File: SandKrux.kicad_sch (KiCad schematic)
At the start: 119 parts, among them CN2 1.25mm-2P socket, IC1 TROPIC01_chip, Q1 S8050, Q2 SI2301CDS-T1-GE3, SW1 TL3330AF130QG, SW2 TL3330AF130QG, SW3 TL3330AF130QG, SW4 TL3330AF130QG, SW5 TL3330AF130QG, U10 AXP173_C3345106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

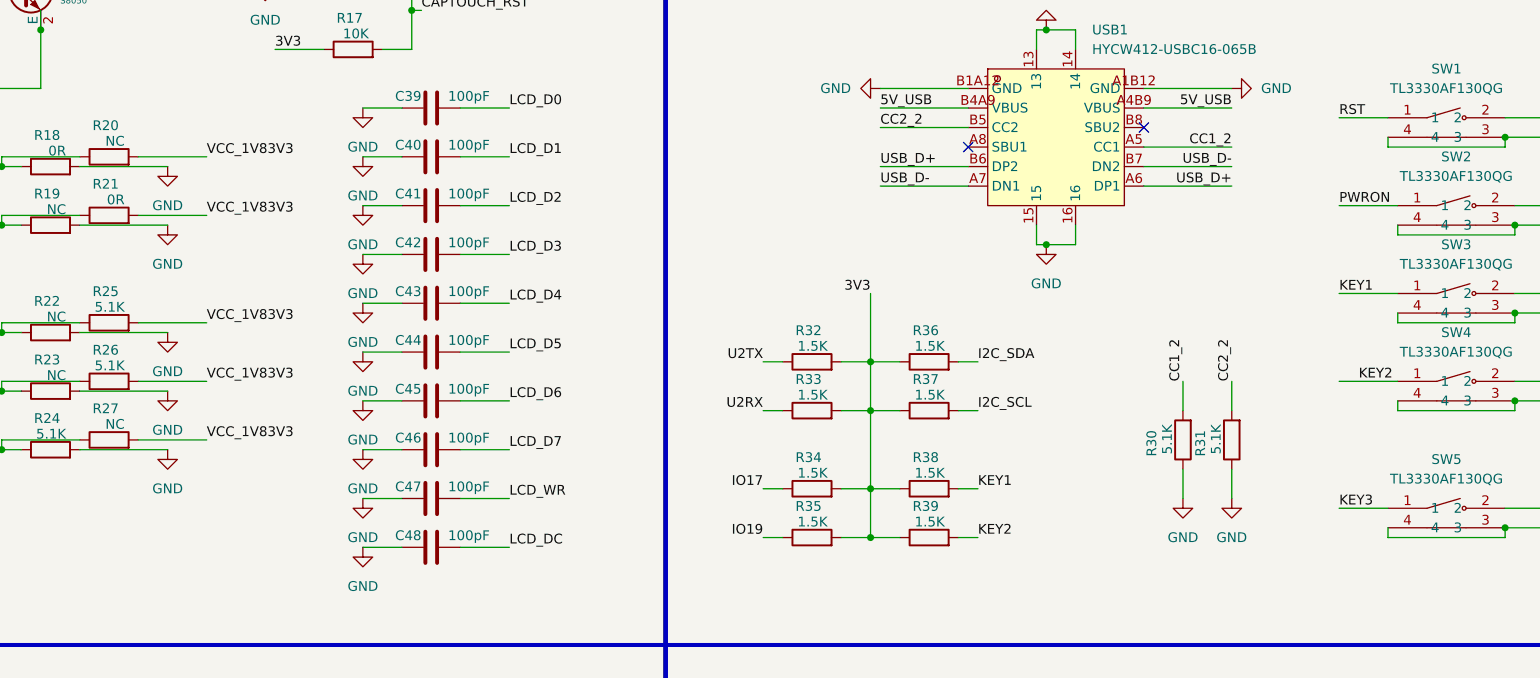
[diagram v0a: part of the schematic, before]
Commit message: lcd and bottons conection on board
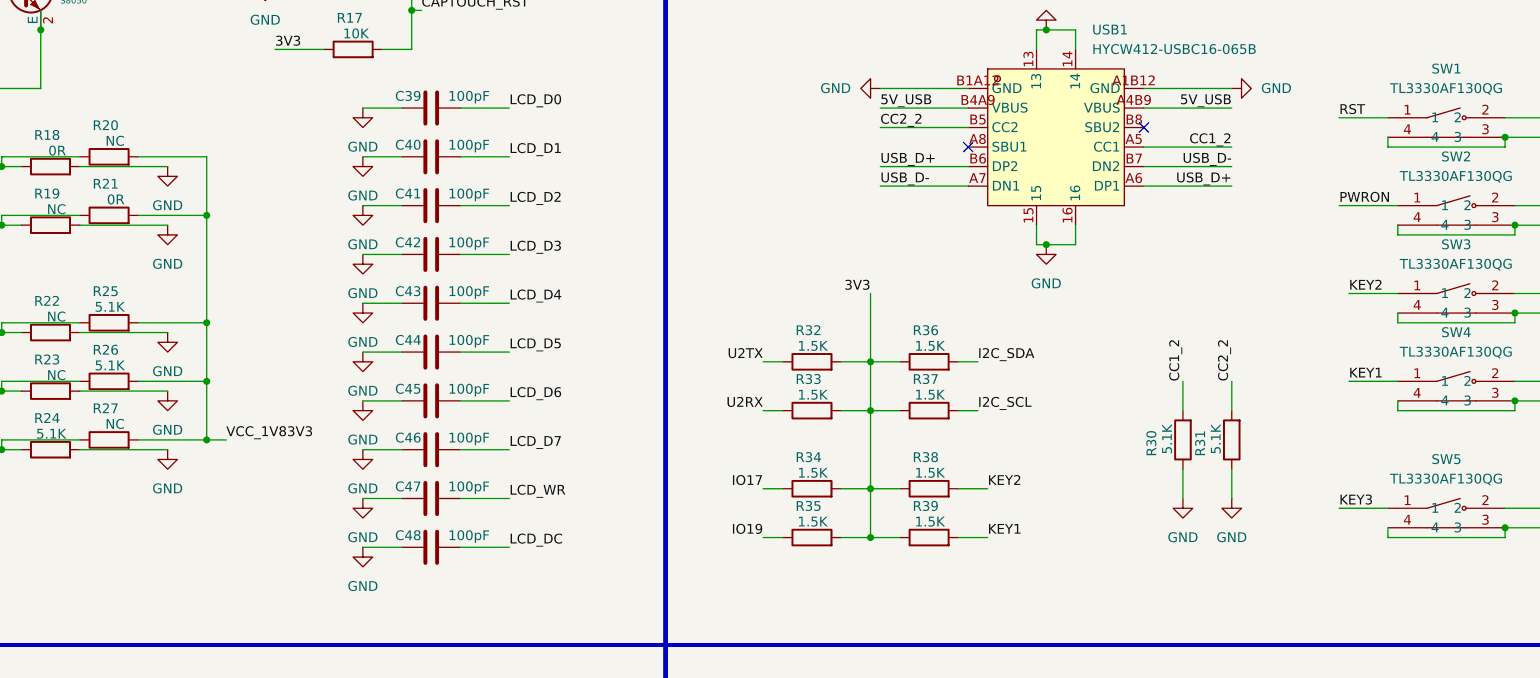
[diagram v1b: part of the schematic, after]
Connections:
- net KEY1: now also R39.2, SW4.1; no longer R38.2, SW3.1
- net KEY2: now also R38.2, SW3.1; no longer R39.2, SW4.1
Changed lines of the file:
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@@
 	)
 	(junction
+		(at 374.65 128.27)
+		(diameter 0)
+		(color 0 0 0 0)
+	)
+	(junction
 		(at 513.08 199.39)
 		(diameter 0)
@@
 	)
 	(junction
+		(at 374.65 106.68)
+		(diameter 0)
+		(color 0 0 0 0)
+	)
+	(junction
 		(at 543.56 147.32)
 		(diameter 0)
@@
 	)
 	(junction
+		(at 374.65 135.89)
+		(diameter 0)
+		(color 0 0 0 0)
+	)
+	(junction
 		(at 283.21 196.85)
 		(diameter 0)
@@
 		(color 0 0 0 0)
 	)
+	(junction
+		(at 374.65 120.65)
+		(diameter 0)
+		(color 0 0 0 0)
+	)
 	(no_connect
 		(at 162.56 39.37)
@@
 	(wire
 		(pts
-			(xy 472.44 142.24) (xy 474.98 142.24)
-		)
-		(stroke
-			(width 0)
-			(type default)
-		)
-	)
-	(wire
-		(pts
 			(xy 513.08 199.39) (xy 515.62 199.39)
 		)
@@
 	(wire
 		(pts
+			(xy 523.24 128.27) (xy 529.59 128.27)
+		)
+		(stroke
+			(width 0)
+			(type default)
+		)
+	)
+	(wire
+		(pts
 			(xy 341.63 229.87) (xy 359.41 229.87)
 		)
@@
 	(wire
 		(pts
+			(xy 377.19 135.89) (xy 374.65 135.89)
+		)
+		(stroke
+			(width 0)
+			(type default)
+		)
+	)
+	(wire
+		(pts
 			(xy 543.56 96.52) (xy 551.18 96.52)
 		)
@@
 	(wire
 		(pts
-			(xy 521.97 116.84) (xy 529.59 116.84)
+			(xy 461.01 142.24) (xy 461.01 148.59)
 		)
 		(stroke
@@
 	(wire
 		(pts
-			(xy 461.01 142.24) (xy 461.01 148.59)
+			(xy 388.62 44.45) (xy 392.43 44.45)
 		)
 		(stroke
@@
 	(wire
 		(pts
-			(xy 388.62 44.45) (xy 392.43 44.45)
+			(xy 397.51 76.2) (xy 401.32 76.2)
 		)
 		(stroke
@@
 	(wire
 		(pts
-			(xy 397.51 76.2) (xy 401.32 76.2)
+			(xy 394.97 92.71) (xy 400.05 92.71)
 		)
 		(stroke
@@
 	(wire
 		(pts
-			(xy 394.97 92.71) (xy 400.05 92.71)
+			(xy 462.28 90.17) (xy 473.71 90.17)
 		)
 		(stroke
@@
 	(wire
 		(pts
-			(xy 462.28 90.17) (xy 473.71 90.17)
+			(xy 472.44 148.59) (xy 476.25 148.59)
 		)
 		(stroke
@@
 	(wire
 		(pts
+			(xy 472.44 142.24) (xy 476.25 142.24)
+		)
+		(stroke
+			(width 0)
+			(type default)
+		)
+	)
+	(wire
+		(pts
 			(xy 303.53 77.47) (xy 312.42 77.47)
 		)
@@
 	(wire
 		(pts
+			(xy 523.24 116.84) (xy 529.59 116.84)
+		)
+		(stroke
+			(width 0)
+			(type default)
+		)
+	)
+	(wire
+		(pts
 			(xy 349.25 201.93) (xy 359.41 201.93)
 		)
@@
 	(wire
 		(pts
-			(xy 303.53 82.55) (xy 312.42 82.55)
-		)
-		(stroke
-			(width 0)
-			(type default)
-		)
-	)
-	(wire
-		(pts
 			(xy 356.87 208.28) (xy 359.41 208.28)
 		)
@@
 	(wire
 		(pts
-			(xy 118.11 109.22) (xy 113.03 109.22)
+			(xy 374.65 120.65) (xy 374.65 128.27)
 		)
 		(stroke
@@
 	(wire
 		(pts
-			(xy 187.96 69.85) (xy 194.31 69.85)
+			(xy 118.11 109.22) (xy 113.03 109.22)
 		)
 		(stroke
@@
 	(wire
 		(pts
-			(xy 425.45 40.64) (xy 427.99 40.64)
+			(xy 187.96 69.85) (xy 194.31 69.85)
 		)
 		(stroke
@@
 	(wire
 		(pts
-			(xy 365.76 135.89) (xy 374.65 135.89)
+			(xy 425.45 40.64) (xy 427.99 40.64)
 		)
 		(stroke
@@
 	(wire
 		(pts
+			(xy 374.65 99.06) (xy 374.65 106.68)
+		)
+		(stroke
+			(width 0)
+			(type default)
+		)
+	)
+	(wire
+		(pts
 			(xy 347.98 264.16) (xy 341.63 264.16)
 		)
@@
 	(wire
 		(pts
+			(xy 374.65 128.27) (xy 374.65 135.89)
+		)
+		(stroke
+			(width 0)
+			(type default)
+		)
+	)
+	(wire
+		(pts
 			(xy 306.07 246.38) (xy 283.21 246.38)
 		)
@@
 	(wire
 		(pts
-			(xy 521.97 128.27) (xy 529.59 128.27)
-		)
-		(stroke
-			(width 0)
-			(type default)
-		)
-	)
-	(wire
-		(pts
 			(xy 557.53 144.78) (xy 557.53 151.13)
 		)
@@
 	(wire
 		(pts
-			(xy 472.44 148.59) (xy 474.98 148.59)
-		)
-		(stroke
-			(width 0)
-			(type default)
-		)
-	)
-	(wire
-		(pts
 			(xy 359.41 198.12) (xy 360.68 198.12)
 		)
@@
 	(wire
 		(pts
+			(xy 374.65 106.68) (xy 374.65 120.65)
+		)
+		(stroke
+			(width 0)
+			(type default)
+		)
+	)
+	(wire
+		(pts
 			(xy 107.95 67.31) (xy 137.16 67.31)
 		)
@@
 	(wire
 		(pts
+			(xy 303.53 82.55) (xy 312.42 82.55)
+		)
+		(stroke
+			(width 0)
+			(type default)
+		)
+	)
+	(wire
+		(pts
 			(xy 510.54 250.19) (xy 508 250.19)
 		)
@@
 	(wire
 		(pts
+			(xy 374.65 135.89) (xy 365.76 135.89)
+		)
+		(stroke
+			(width 0)
+			(type default)
+		)
+	)
+	(wire
+		(pts
 			(xy 95.25 30.48) (xy 106.68 30.48)
 		)
@@
 		)
 	)
-	(label "VCC_1V83V3"
-		(at 374.65 128.27 0)
-		(effects
-			(font
-				(size 1.27 1.27)
-			)
-			(justify left bottom)
-		)
-	)
 	(label "USB_D+"
 		(at 462.28 100.33 0)
@@
 	)
 	(label "KEY2"
-		(at 474.98 148.59 0)
+		(at 476.25 142.24 0)
 		(effects
 			(font
@@
 	)
 	(label "KEY1"
-		(at 521.97 116.84 0)
+		(at 523.24 128.27 0)
 		(effects
 			(font
@@
 	)
 	(label "KEY2"
-		(at 524.51 128.27 0)
+		(at 523.24 116.84 0)
 		(effects
 			(font
@@
 	)
 	(label "VCC_1V83V3"
-		(at 374.65 135.89 0)
+		(at 377.19 135.89 0)
 		(effects
 			(font
@@
 		)
 	)
-	(label "VCC_1V83V3"
-		(at 374.65 120.65 0)
-		(effects
-			(font
-				(size 1.27 1.27)
-			)
-			(justify left bottom)
-		)
-	)
 	(label "24M_OUT"
 		(at 130.81 62.23 180)
@@
 		)
 	)
-	(label "VCC_1V83V3"
-		(at 374.65 106.68 0)
-		(effects
-			(font
-				(size 1.27 1.27)
-			)
-			(justify left bottom)
-		)
-	)
-	(label "VCC_1V83V3"
-		(at 374.65 99.06 0)
-		(effects
-			(font
-				(size 1.27 1.27)
-			)
-			(justify left bottom)
-		)
-	)
 	(label "GD_PA1"
 		(at 130.81 72.39 180)
@@
 	)
 	(label "KEY1"
-		(at 474.98 142.24 0)
+		(at 476.25 148.59 0)
 		(effects
 			(font

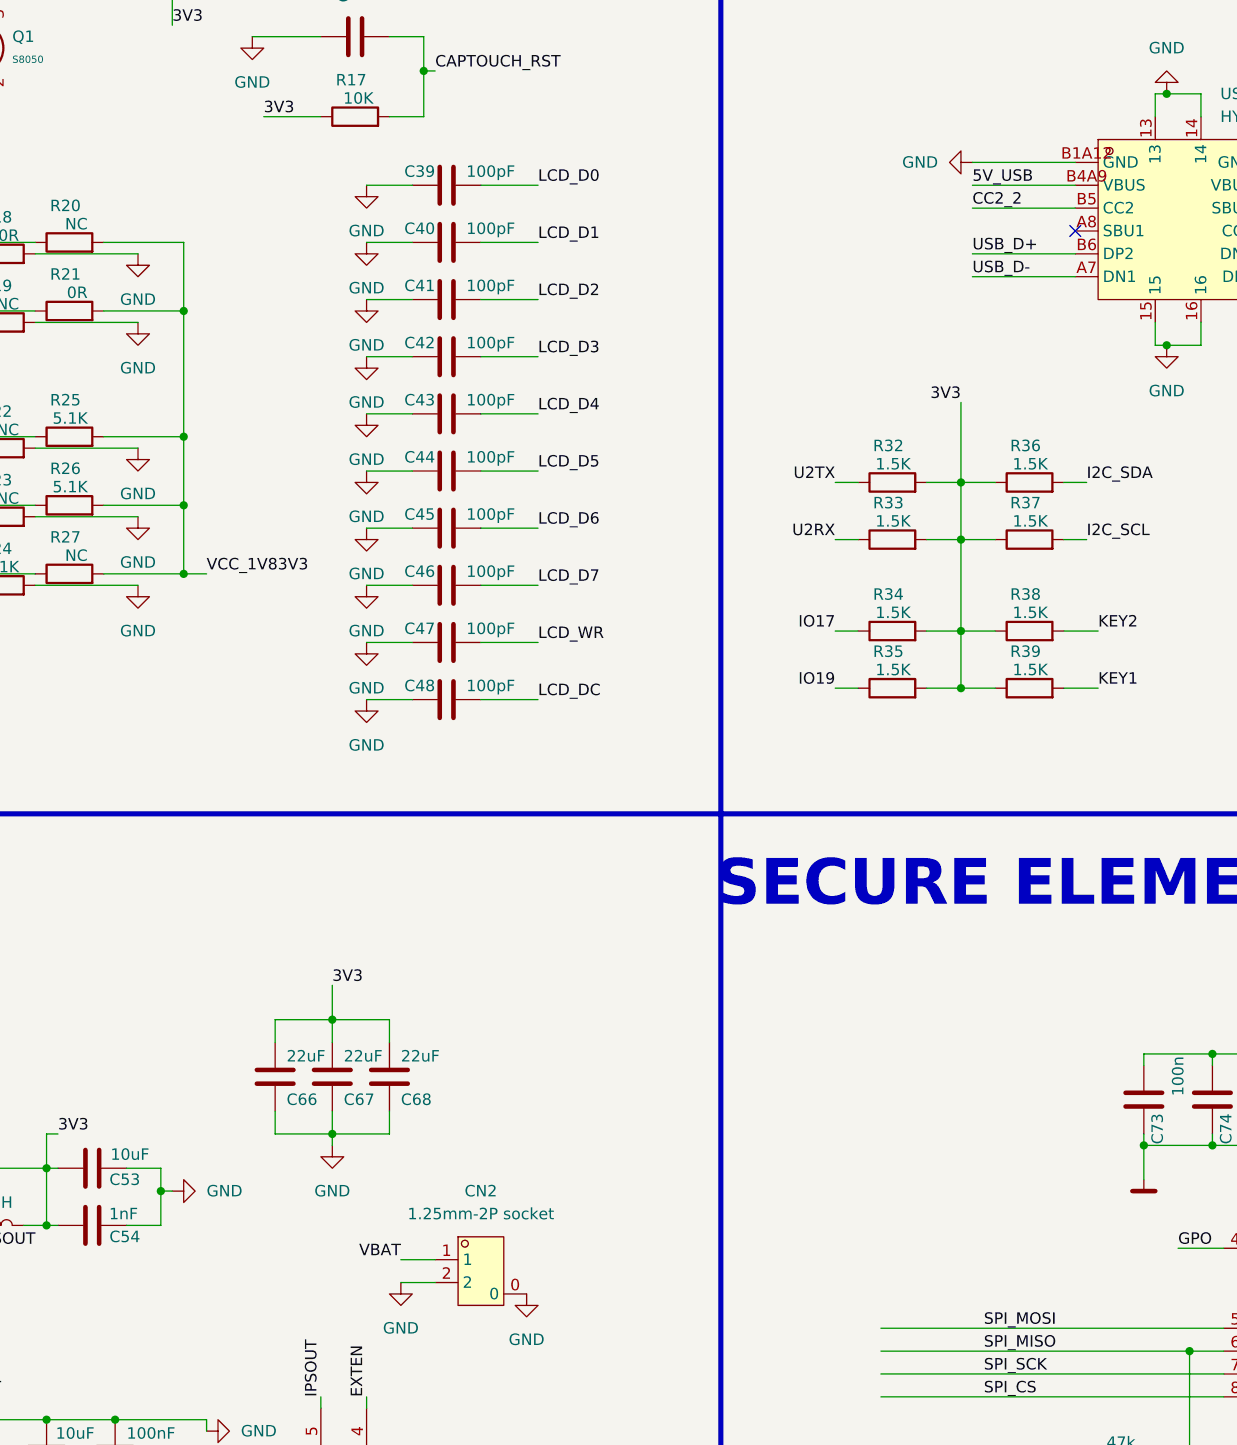
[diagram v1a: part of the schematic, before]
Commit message: test points and traces distribution
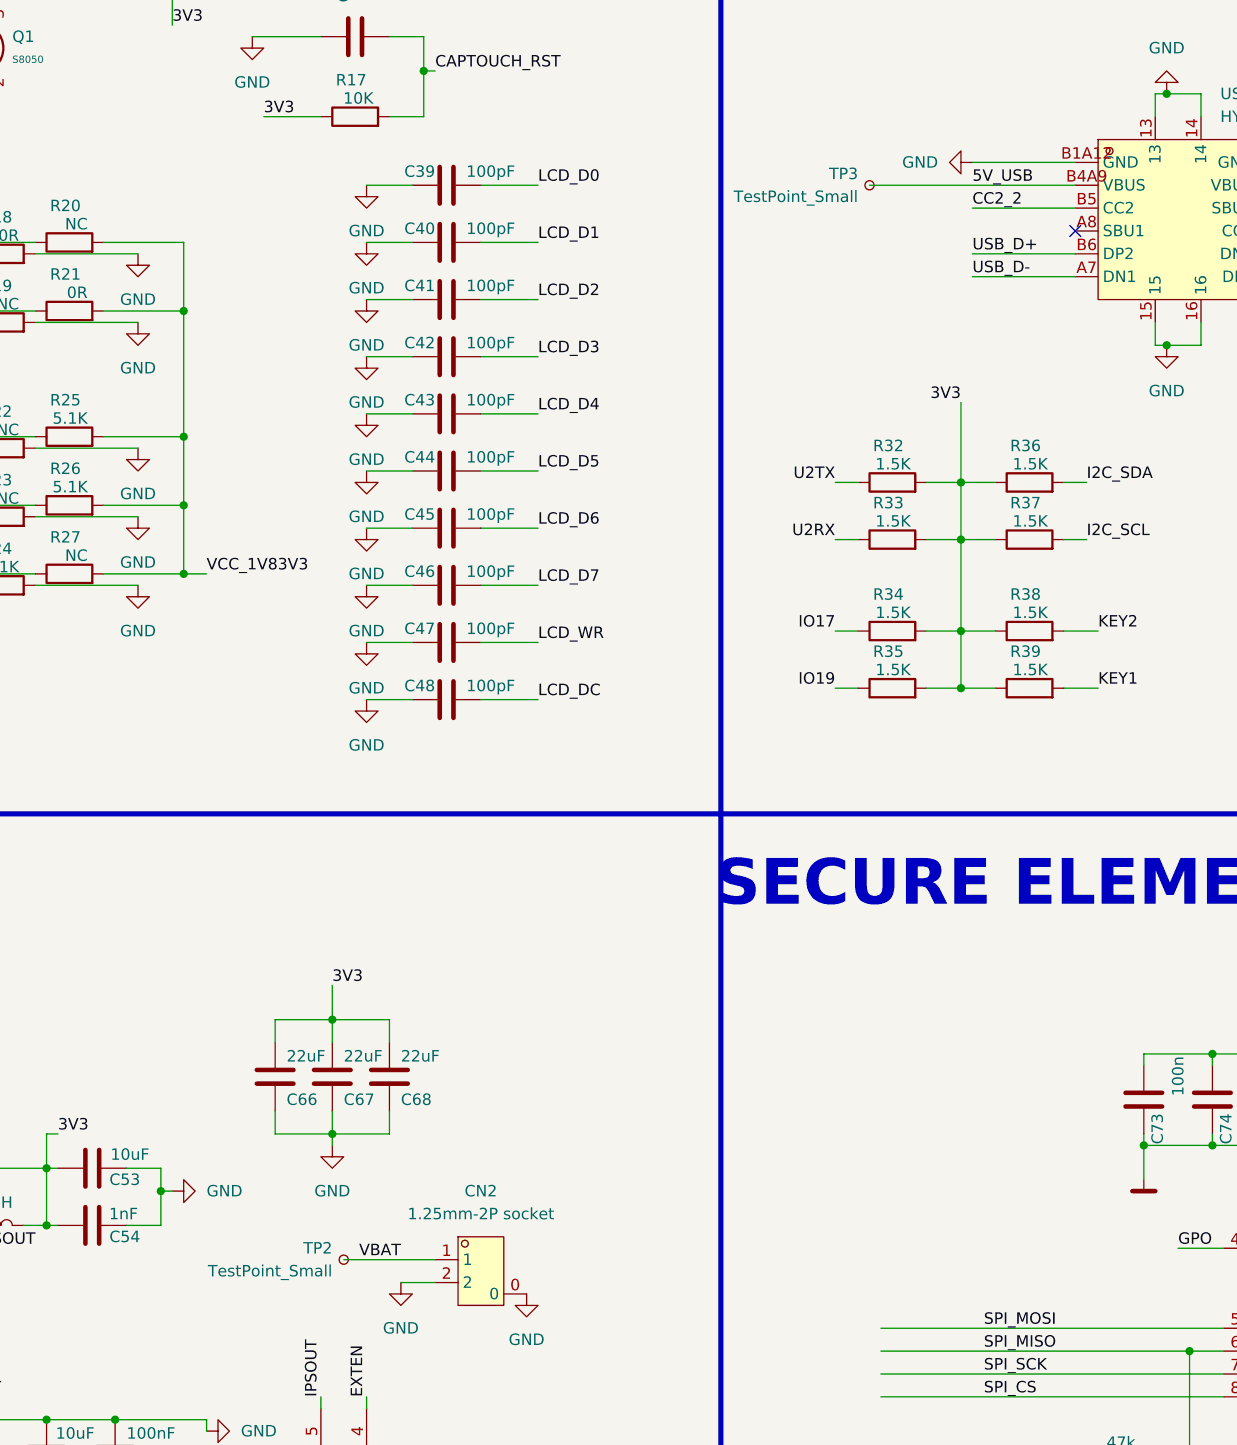
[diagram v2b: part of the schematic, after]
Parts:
- added TP2, TP3: TestPoint_Small, TestPoint:TestPoint_Pad_D1.0mm, symbol Connector:TestPoint_Small
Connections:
- net 5V_USB: now also TP3.1
- net VBAT: now also TP2.1
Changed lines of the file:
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@@
 	(wire
 		(pts
-			(xy 398.78 212.09) (xy 402.59 212.09)
-		)
-		(stroke
-			(width 0)
-			(type default)
-		)
-	)
-	(wire
-		(pts
 			(xy 283.21 205.74) (xy 283.21 204.47)
 		)
@@
 	(wire
 		(pts
+			(xy 392.43 212.09) (xy 402.59 212.09)
+		)
+		(stroke
+			(width 0)
+			(type default)
+		)
+	)
+	(wire
+		(pts
 			(xy 518.16 250.19) (xy 515.62 250.19)
 		)
@@
 	(wire
 		(pts
+			(xy 450.85 92.71) (xy 473.71 92.71)
+		)
+		(stroke
+			(width 0)
+			(type default)
+		)
+	)
+	(wire
+		(pts
 			(xy 170.18 90.17) (xy 170.18 99.06)
 		)
@@
 	(wire
 		(pts
-			(xy 462.28 92.71) (xy 473.71 92.71)
-		)
-		(stroke
-			(width 0)
-			(type default)
-		)
-	)
-	(wire
-		(pts
 			(xy 359.41 201.93) (xy 359.41 208.28)
 		)
@@
 	)
 	(symbol
+		(lib_id "Connector:TestPoint_Small")
+		(at 450.85 92.71 0)
+		(mirror y)
+		(unit 1)
+		(exclude_from_sim no)
+		(in_bom yes)
+		(on_board yes)
+		(dnp no)
+		(property "Reference" "TP3"
+			(at 449.58 91.4399 0)
+			(effects
+				(font
+					(size 1.27 1.27)
+				)
+				(justify left)
+			)
+		)
+		(property "Value" "TestPoint_Small"
+			(at 449.58 93.9799 0)
+			(effects
+				(font
+					(size 1.27 1.27)
+				)
+				(justify left)
+			)
+		)
+		(property "Footprint" "TestPoint:TestPoint_Pad_D1.0mm"
+			(at 445.77 92.71 0)
+			(effects
+				(font
+					(size 1.27 1.27)
+				)
+				(hide yes)
+			)
+		)
+		(property "Datasheet" "~"
+			(at 445.77 92.71 0)
+			(effects
+				(font
+					(size 1.27 1.27)
+				)
+				(hide yes)
+			)
+		)
+		(property "Description" "test point"
+			(at 450.85 92.71 0)
+			(effects
+				(font
+					(size 1.27 1.27)
+				)
+				(hide yes)
+			)
+		)
+		(pin "1"
+		)
+		(instances
+			(project "SandKrux"
+				(path "/0986b4b2-29ef-45bb-b940-2ffd44ad7a0e"
+					(reference "TP3")
+					(unit 1)
+				)
+			)
+		)
+	)
+	(symbol
 		(lib_id "Device:R")
 		(at 218.44 66.04 90)
@@
 					(unit 1)
 				)
+			)
+		)
+	)
+	(symbol
+		(lib_id "Connector:TestPoint_Small")
+		(at 392.43 212.09 0)
+		(mirror y)
+		(unit 1)
+		(exclude_from_sim no)
+		(in_bom yes)
+		(on_board yes)
+		(dnp no)
+		(property "Reference" "TP2"
+			(at 391.16 210.8199 0)
+			(effects
+				(font
+					(size 1.27 1.27)
+				)
+				(justify left)
+			)
+		)
+		(property "Value" "TestPoint_Small"
+			(at 391.16 213.3599 0)
+			(effects
+				(font
+					(size 1.27 1.27)
+				)
+				(justify left)
+			)
+		)
+		(property "Footprint" "TestPoint:TestPoint_Pad_D1.0mm"
+			(at 387.35 212.09 0)
+			(effects
+				(font
+					(size 1.27 1.27)
+				)
+				(hide yes)
+			)
+		)
+		(property "Datasheet" "~"
+			(at 387.35 212.09 0)
+			(effects
+				(font
+					(size 1.27 1.27)
+				)
+				(hide yes)
+			)
+		)
+		(property "Description" "test point"
+			(at 392.43 212.09 0)
+			(effects
+				(font
+					(size 1.27 1.27)
+				)
+				(hide yes)
+			)
+		)
+		(pin "1"
+		)
+		(instances
+			(project "SandKrux"
+				(path "/0986b4b2-29ef-45bb-b940-2ffd44ad7a0e"
+					(reference "TP2")
+					(unit 1)
+				)
